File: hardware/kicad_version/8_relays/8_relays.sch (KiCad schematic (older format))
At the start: 78 parts, among them K101 CONN_3, K102 J_IN, K103 CONN_3, K104 J_OUT, K105 G5LA-1-12VDC, K106 G5LA-1-12VDC, K107 G5LA-1-12VDC, K108 G5LA-1-12VDC, K109 G5LA-1-12VDC, K110 G5LA-1-12VDC, K111 G5LA-1-12VDC, K112 G5LA-1-12VDC, K113 CONN_3, K114 CONN_3, K115 CONN_3, K116 CONN_3, K117 CONN_3, K118 CONN_3, K119 CONN_3, K120 CONN_3, Q101 DSS20201L NPN, Q102 DSS20201L NPN, Q103 DSS20201L NPN, Q104 DSS20201L NPN, Q105 DSS20201L NPN, Q106 DSS20201L NPN, Q107 DSS20201L NPN, Q108 DSS20201L NPN, Q109 MMBT2222A, Q110 MMBT2222A, Q111 MMBT2222A, Q112 MMBT2222A, Q113 MMBT2222A, Q114 MMBT2222A, Q115 MMBT2222A, Q116 MMBT2222A, U101 74HC595

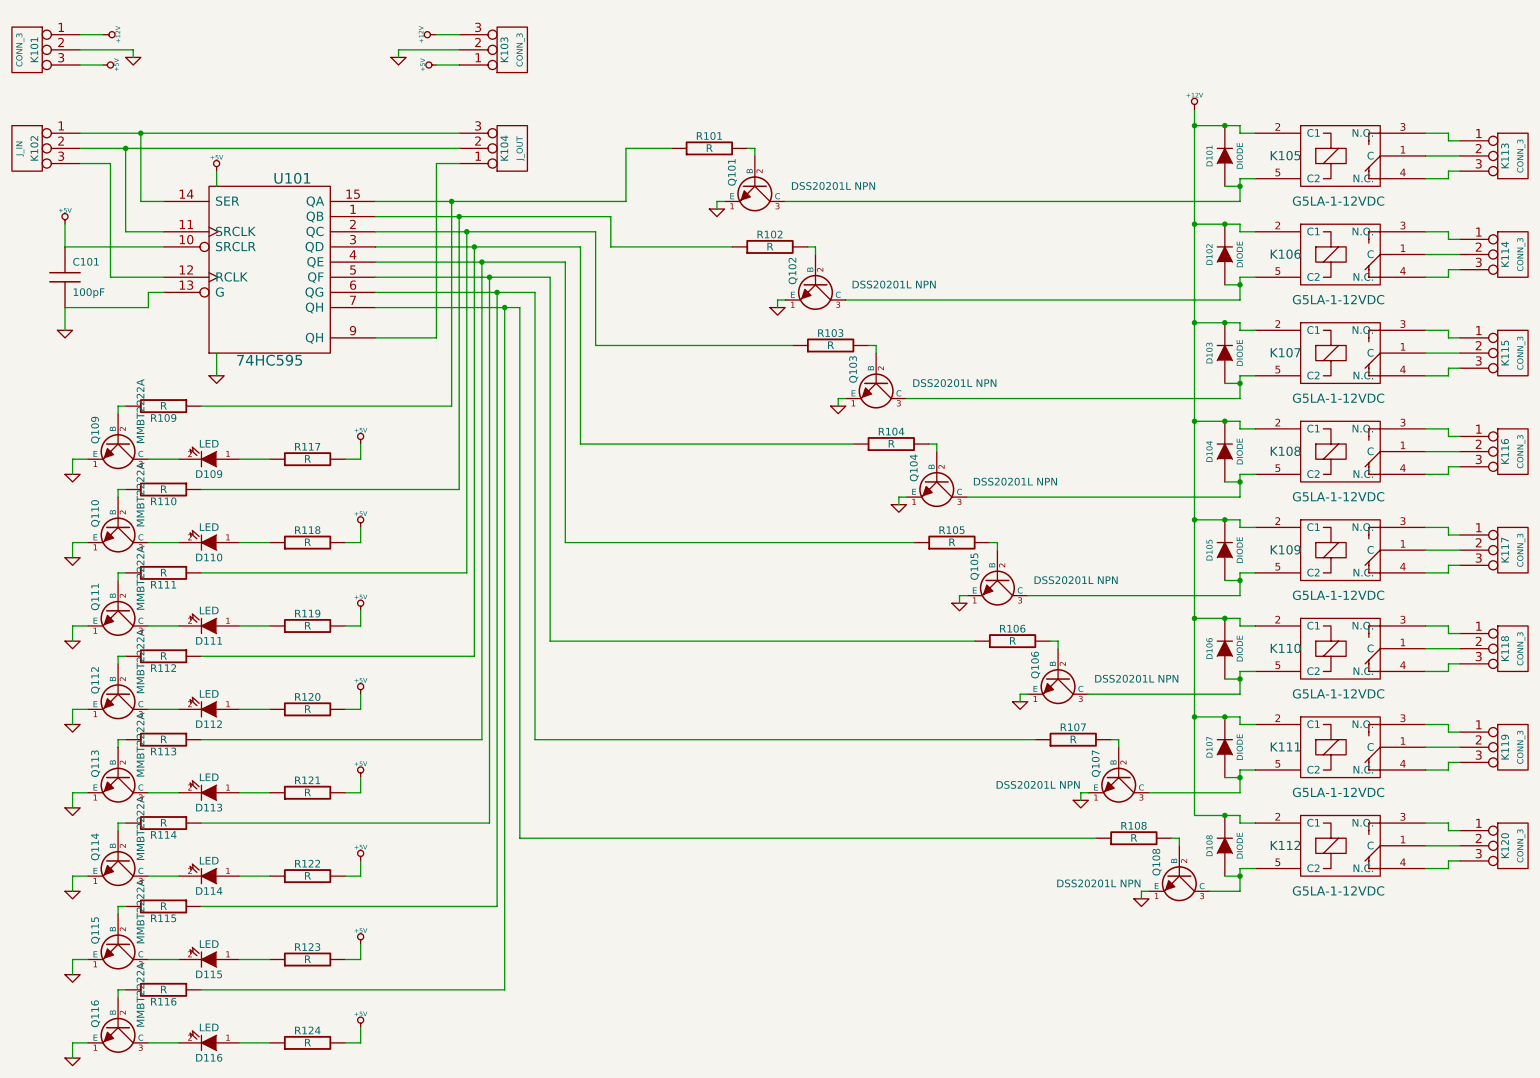
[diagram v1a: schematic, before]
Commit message: Dossier contenant les versions stable hardware et software
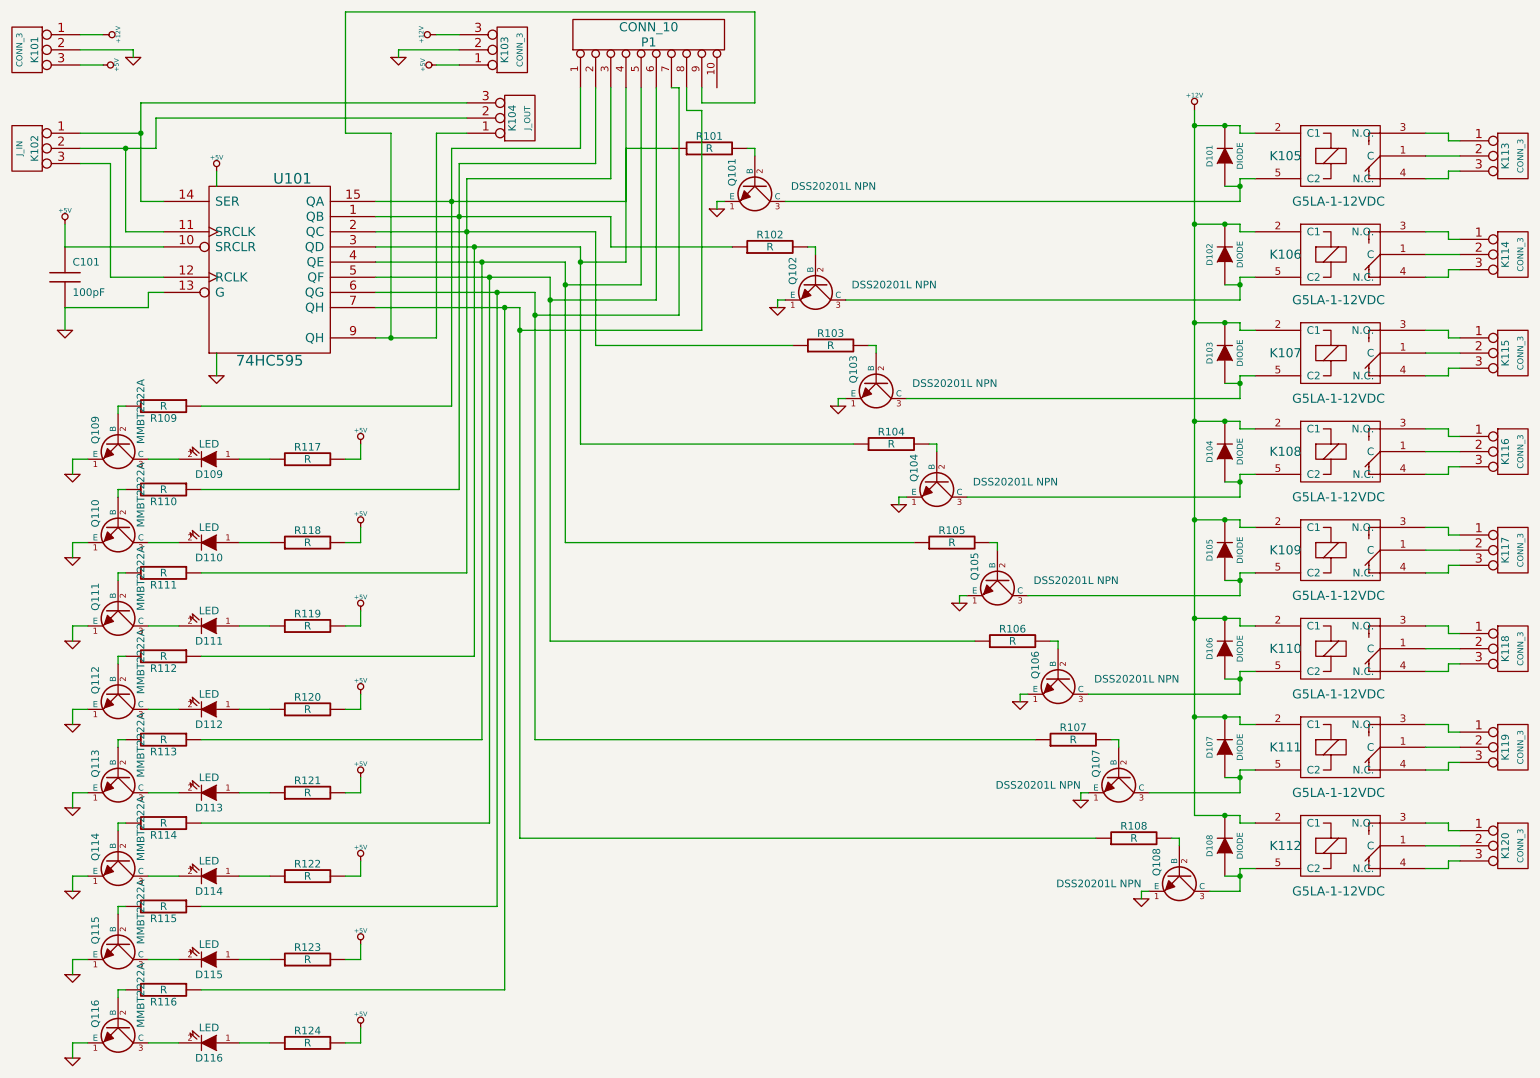
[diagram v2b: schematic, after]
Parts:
- added P1: CONN_10, symbol CONN_10
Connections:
- net at R102.1, R110.1, U101.1 (QB): now also P1.2 (P2)
- net at R101.1, R109.1, U101.15 (QA): now also R104.1, R112.1, U101.3 (QD), P1.1 (P1), P1.4 (P4)
- net at R103.1, R111.1, U101.2 (QC): now also P1.3 (P3)
- net at R105.1, R113.1, U101.4 (QE): now also P1.5 (P5)
- net at R106.1, R114.1, U101.5 (QF): now also P1.6 (P6)
- net at R107.1, R115.1, U101.6 (QG): now also P1.7 (P7)
- net at R108.1, R116.1, U101.7 (QH): now also P1.8 (P8)
- net at K104.1 (P1), U101.9 (QH): now also P1.9 (P9)
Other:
- moved on the sheet: K104
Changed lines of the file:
@@
-EESchema Schematic File Version 2  date 01/04/2012 14:12:18
+EESchema Schematic File Version 2  date jeu. 12 avril 2012 23:20:10 CEST
 LIBS:power
 LIBS:device
@@
 Sheet 1 1
 Title ""
-Date "1 apr 2012"
+Date "12 apr 2012"
 Rev ""
 Comp ""
@@
 Comment4 ""
 $EndDescr
+Wire Wire Line
+	5200 1000 5200 1100
+Wire Wire Line
+	5200 1100 5550 1100
+Wire Wire Line
+	5550 1100 5550 500
+Wire Wire Line
+	5550 500  2850 500
+Wire Wire Line
+	2850 500  2850 1300
+Wire Wire Line
+	2850 1300 3150 1300
+Connection ~ 3150 2650
+Wire Wire Line
+	3150 1300 3150 2650
+Wire Wire Line
+	5000 1000 5050 1000
+Wire Wire Line
+	5050 1000 5050 2500
+Connection ~ 4100 2500
+Wire Wire Line
+	5050 2500 4100 2500
+Wire Wire Line
+	4800 1000 4800 2300
+Connection ~ 4300 2300
+Wire Wire Line
+	4800 2300 4300 2300
+Wire Wire Line
+	4600 1000 4600 1600
+Wire Wire Line
+	4600 1600 3650 1600
+Wire Wire Line
+	3650 1600 3650 4200
+Wire Wire Line
+	4400 1000 4400 1400
+Wire Wire Line
+	4400 1400 3550 1400
+Wire Wire Line
+	3550 1400 3550 3100
+Wire Wire Line
+	4600 1850 4600 2050
+Wire Wire Line
+	4400 2050 4400 3350
+Wire Wire Line
+	4200 2250 4200 4650
+Wire Wire Line
+	4000 2450 4000 5950
+Wire Wire Line
+	3650 1200 1600 1200
+Wire Wire Line
+	1600 1200 1600 1400
+Wire Wire Line
+	1600 1400 1100 1400
+Wire Wire Line
+	1100 1300 1500 1300
 Connection ~ 3900 2450
 Wire Wire Line
@@
 Connection ~ 3600 1850
 Wire Wire Line
-	3600 1850 3600 3650
-Wire Wire Line
-	3600 3650 1900 3650
+	1900 3650 3600 3650
 Connection ~ 3550 1750
 Wire Wire Line
-	3550 1750 3550 3100
-Wire Wire Line
 	2150 7300 2350 7300
 Wire Wire Line
@@
 	7400 5300 4100 5300
 Wire Wire Line
-	4100 5300 4100 2350
-Wire Wire Line
-	4100 2350 3050 2350
+	3050 2350 4100 2350
 Wire Wire Line
 	6600 4000 4300 4000
 Wire Wire Line
-	4300 4000 4300 2150
-Wire Wire Line
-	4300 2150 3050 2150
+	3050 2150 4300 2150
 Wire Wire Line
 	5800 2700 4500 2700
 Wire Wire Line
-	4500 2700 4500 1950
-Wire Wire Line
-	4500 1950 3050 1950
+	3050 1950 4500 1950
 Wire Wire Line
 	5000 1400 4700 1400
 Wire Wire Line
-	4700 1400 4700 1750
-Wire Wire Line
-	4700 1750 3050 1750
+	3050 1750 4700 1750
 Wire Wire Line
 	5950 2100 5950 2050
@@
 	8850 3550 8750 3550
 Wire Wire Line
-	8750 3600 8650 3600
+	8650 3600 8750 3600
 Wire Wire Line
 	8750 2250 8850 2250
@@
 	8850 1600 8750 1600
 Wire Wire Line
-	8750 1650 8650 1650
+	8650 1650 8750 1650
 Wire Wire Line
 	8850 6150 8750 6150
 Wire Wire Line
-	8750 6200 8650 6200
+	8650 6200 8750 6200
 Wire Wire Line
 	8850 5200 8750 5200
@@
 Connection ~ 1500 1300
 Wire Wire Line
-	3600 1300 1100 1300
-Wire Wire Line
-	3600 1500 3450 1500
-Wire Wire Line
-	3450 1500 3450 2650
-Wire Wire Line
-	3450 2650 3050 2650
+	3050 2650 3450 2650
 Wire Wire Line
 	1650 1950 1400 1950
@@
 	1000 2450 1000 2600
 Wire Wire Line
-	1500 1300 1500 1750
-Wire Wire Line
-	1500 1750 1650 1750
+	1650 1750 1500 1750
 Wire Wire Line
 	1100 1500 1300 1500
@@
 Wire Wire Line
 	1300 2250 1650 2250
-Wire Wire Line
-	3600 1400 1100 1400
 Connection ~ 1400 1400
 Wire Wire Line
@@
 	8750 3250 8850 3250
 Wire Wire Line
-	8750 2950 8650 2950
+	8650 2950 8750 2950
 Wire Wire Line
 	8850 2900 8750 2900
@@
 	5700 2400 5700 2450
 Wire Wire Line
-	3050 1850 4600 1850
-Wire Wire Line
-	4600 1850 4600 2050
+	4600 1850 3050 1850
 Wire Wire Line
 	4600 2050 5400 2050
 Wire Wire Line
-	3050 2050 4400 2050
-Wire Wire Line
-	4400 2050 4400 3350
+	4400 2050 3050 2050
 Wire Wire Line
 	4400 3350 6200 3350
 Wire Wire Line
-	3050 2250 4200 2250
-Wire Wire Line
-	4200 2250 4200 4650
+	4200 2250 3050 2250
 Wire Wire Line
 	4200 4650 7000 4650
 Wire Wire Line
-	3050 2450 4000 2450
-Wire Wire Line
-	4000 2450 4000 5950
+	4000 2450 3050 2450
 Wire Wire Line
 	4000 5950 7800 5950
@@
 Connection ~ 3750 2150
 Wire Wire Line
-	1900 4200 3650 4200
-Wire Wire Line
-	3650 4200 3650 1950
+	3650 4200 1900 4200
 Wire Wire Line
 	1900 5300 3750 5300
@@
 	3850 6400 3850 2350
 Connection ~ 3850 2350
+Wire Wire Line
+	1500 1750 1500 1100
+Wire Wire Line
+	1500 1100 3650 1100
+Wire Wire Line
+	3650 1300 3450 1300
+Wire Wire Line
+	4100 2350 4100 5300
+Wire Wire Line
+	4500 1950 4500 2700
+Wire Wire Line
+	4700 1750 4700 1400
+Wire Wire Line
+	3450 1300 3450 2650
+Wire Wire Line
+	4300 2150 4300 4000
+Wire Wire Line
+	3600 3650 3600 1500
+Wire Wire Line
+	3600 1500 4500 1500
+Wire Wire Line
+	4500 1500 4500 1000
+Wire Wire Line
+	4700 1000 4700 2150
+Wire Wire Line
+	4700 2150 4400 2150
+Connection ~ 4400 2150
+Wire Wire Line
+	4200 2400 4900 2400
+Connection ~ 4200 2400
+Wire Wire Line
+	4900 2400 4900 1000
+Wire Wire Line
+	4000 2600 5200 2600
+Connection ~ 4000 2600
+Wire Wire Line
+	5200 2600 5200 1150
+Wire Wire Line
+	5200 1150 5100 1150
+Wire Wire Line
+	5100 1150 5100 1000
+$Comp
+L CONN_10 P1
+U 1 1 4F874664
+P 4850 650
+F 0 "P1" V 4800 650 60  0000 C CNN
+F 1 "CONN_10" V 4900 650 60  0000 C CNN
+	1    4850 650
+	0    -1   -1   0
+$EndComp
 $Comp
 L R R109
@@
 L CONN_3 K104
 U 1 1 4F455C15
-P 3950 1400
-F 0 "K104" V 3900 1400 50  0000 C CNN
-F 1 "J_OUT" V 4000 1400 40  0000 C CNN
-	1    3950 1400
+P 4000 1200
+F 0 "K104" V 3950 1200 50  0000 C CNN
+F 1 "J_OUT" V 4050 1200 40  0000 C CNN
+	1    4000 1200
 	1    0    0    1
 $EndComp
